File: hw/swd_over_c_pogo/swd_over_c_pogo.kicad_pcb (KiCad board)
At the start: 2 copper layers, 20.5 x 11 mm, 8 parts, among them J1 Conn_01x06

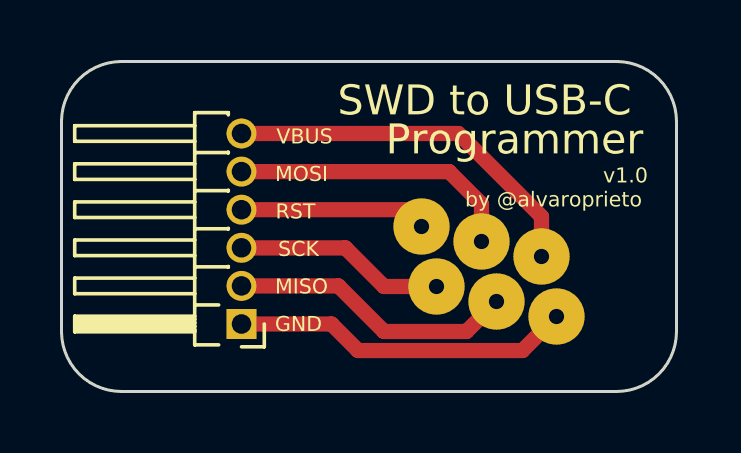
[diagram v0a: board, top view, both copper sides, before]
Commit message: Updated swd over c to v1.1 (and programmer)
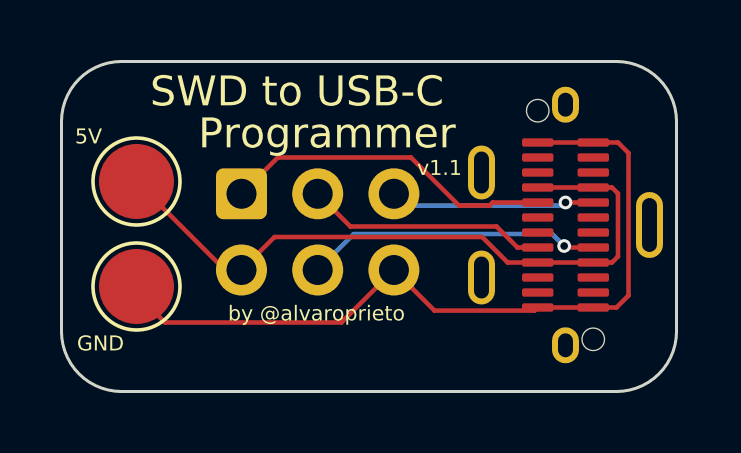
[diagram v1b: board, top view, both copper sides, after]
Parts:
- removed REF**: OSHW-Symbol_6.7x6mm_SilkScreen, Symbol:OSHW-Symbol_6.7x6mm_SilkScreen
- removed TP3: SCK, alvarop:0906-3-15-20-75-14-11-0
- removed TP4: MISO, alvarop:0906-3-15-20-75-14-11-0
- removed TP5: MOSI, alvarop:0906-3-15-20-75-14-11-0
- removed TP6: NRST, alvarop:0906-3-15-20-75-14-11-0
- added P1: USB_C_Plug, alvarop:USB4151-GF-C, F.Cu at (175.8, 67.5)
- J1: value Conn_01x06 -> AVR-ISP-6; footprint Connector_PinHeader_1.27mm:PinHeader_1x06_P1.27mm_Horizontal -> Connector_IDC:IDC-Header_2x03_P2.54mm_Vertical; moved to B.Cu
- TP1: value VBUS -> TestPoint; footprint alvarop:0906-3-15-20-75-14-11-0 -> TestPoint:TestPoint_Pad_D2.5mm
- TP2: value GND -> TestPoint; footprint alvarop:0906-3-15-20-75-14-11-0 -> TestPoint:TestPoint_Pad_D2.5mm
- moved TP2 14.0 mm to (161.5, 69.5), turned to -90 degrees
- moved TP1 13.7 mm to (161.5, 66.0), turned to -90 degrees
- moved J1 4.34 mm to (165.0, 66.4), turned to -90 degrees
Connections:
- J1 pad 1: GND -> /MISO
- J1 pad 2: /MISO -> VBUS
- J1 pad 4: /MCURST -> /MOSI
- J1 pad 5: /MOSI -> /MCURST
- J1 pad 6: VBUS -> GND
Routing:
- net GND: track 11.3 -> 25.9 mm
- net VBUS: track 12.5 -> 23.3 mm
- net /MISO: track 9.54 -> 11.1 mm
- net /SCK: track 7.03 -> 8.08 mm
- net /MCURST: track 6.23 -> 6.85 mm, vias 0 -> 1
- net /MOSI: track 9.70 -> 9.87 mm, vias 0 -> 1
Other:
- board text added: "5V"
- board text added: "v1.1"
- board text removed: "MISO"
- board text removed: "MOSI"
- board text removed: "RST"
- board text removed: "SCK"
- board text removed: "VBUS"
- board text removed: "v1.0"

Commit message: Switched to 0402 instead of 0201 components
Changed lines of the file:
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@@
     (fp_line (start -1.98 -8.99) (end -1.98 -4.59) (layer "B.Fab") (width 0.1))
     (fp_line (start -1.98 -4.59) (end -3.18 -4.59) (layer "B.Fab") (width 0.1))
-    (pad "1" thru_hole roundrect (at 0 0 270) (size 1.7 1.7) (drill 1) (layers *.Cu *.Mask) (roundrect_rratio 0.147059)
+    (pad "1" thru_hole roundrect (at 0 0 270) (size 1.7 1.7) (drill 1) (layers *.Cu *.Mask) (roundrect_rratio 0.1470588235)
       (net 3 "/MISO") (pinfunction "MISO") (pintype "passive"))
     (pad "2" thru_hole circle (at 2.54 0 270) (size 1.7 1.7) (drill 1) (layers *.Cu *.Mask)

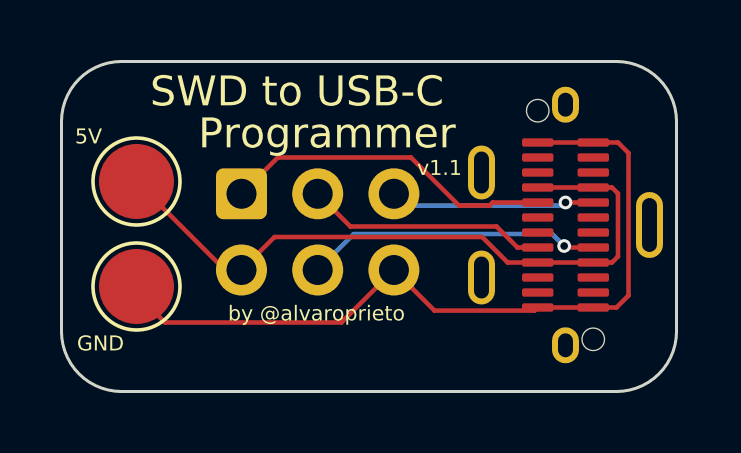
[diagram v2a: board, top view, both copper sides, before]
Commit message: Fixed MISO/MOSI swap and added BOM to swd2usbc
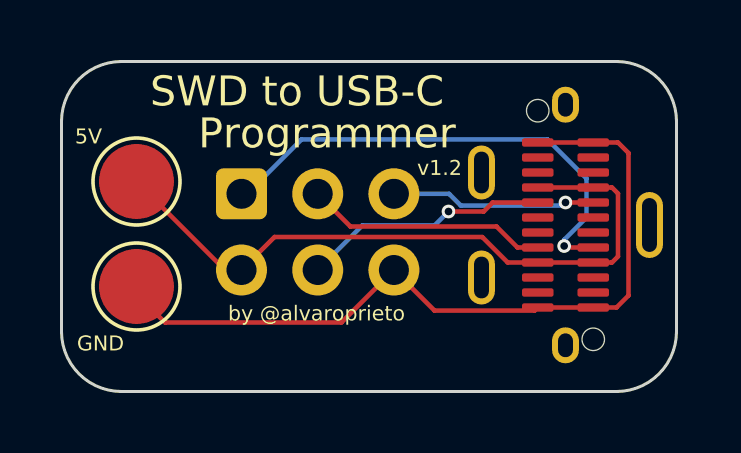
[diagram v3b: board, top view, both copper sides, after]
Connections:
- P1 pad A5: /MISO -> /MOSI
- P1 pad B5: /MOSI -> /MISO
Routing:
- net /MISO: track 11.1 -> 16.3 mm, vias 0 -> 1
- net /MOSI: track 9.87 -> 8.27 mm
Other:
- board text added: "v1.2"
- board text removed: "v1.1"
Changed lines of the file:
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@@
   (title_block
     (title "Debugotron - SWD to USB-C Programmer")
-    (date "2022-02-06")
-    (rev "1.1")
+    (date "2022-03-04")
+    (rev "1.2")
     (company "Quesadillon LLC")
   )
@@
   (footprint "alvarop:USB4151-GF-C" (layer "F.Cu")
     (at 175.8 67.45 90)
+    (property "MPN" " USB4151-GF-C")
     (property "Sheetfile" "swd_over_c_pogo.kicad_sch")
     (property "Sheetname" "")
@@
       (net 1 "VBUS") (pinfunction "VBUS") (pintype "passive"))
     (pad "A5" smd roundrect (at 0.75 -0.925 90) (size 0.28 1.05) (layers "F.Cu" "F.Paste" "F.Mask") (roundrect_rratio 0.25)
-      (net 3 "/MISO") (pinfunction "CC") (pintype "bidirectional"))
+      (net 4 "/MOSI") (pinfunction "CC") (pintype "bidirectional"))
     (pad "A6" smd roundrect (at 0.25 -0.925 90) (size 0.28 1.05) (layers "F.Cu" "F.Paste" "F.Mask") (roundrect_rratio 0.25)
       (net 9 "unconnected-(P1-PadA6)") (pinfunction "D+") (pintype "bidirectional+no_connect"))
@@
       (net 1 "VBUS") (pinfunction "VBUS") (pintype "passive"))
     (pad "B5" smd roundrect (at -0.75 0.925 90) (size 0.28 1.05) (layers "F.Cu" "F.Paste" "F.Mask") (roundrect_rratio 0.25)
-      (net 4 "/MOSI") (pinfunction "VCONN") (pintype "bidirectional"))
+      (net 3 "/MISO") (pinfunction "VCONN") (pintype "bidirectional"))
     (pad "B8" smd roundrect (at 0.75 0.925 90) (size 0.28 1.05) (layers "F.Cu" "F.Paste" "F.Mask") (roundrect_rratio 0.25)
       (net 6 "/MCURST") (pinfunction "SBU2") (pintype "bidirectional"))
@@
     (descr "Through hole IDC box header, 2x03, 2.54mm pitch, DIN 41651 / IEC 60603-13, double rows, https://docs.google.com/spreadsheets/d/16SsEcesNF15N3Lb4niX7dcUr-NY5_MFPQhobNuNppn4/edit#gid=0")
     (tags "Through hole vertical IDC box header THT 2x03 2.54mm double row")
+    (property "MPN" "30306-6002HB")
     (property "Sheetfile" "swd_over_c_pogo.kicad_sch")
     (property "Sheetname" "")
@@
     (effects (font (size 0.5 0.5) (thickness 0.08)))
   )
-  (gr_text "v1.1" (at 171.6 65.55) (layer "F.SilkS")
+  (gr_text "v1.2" (at 171.6 65.55) (layer "F.SilkS")
     (effects (font (size 0.5 0.5) (thickness 0.08)))
   )
@@
   (segment (start 174.875 70.2) (end 176.725 70.2) (width 0.1524) (layer "F.Cu") (net 2))
   (segment (start 171.43272 70.30272) (end 170.08 68.95) (width 0.1524) (layer "F.Cu") (net 2))
-  (segment (start 172.25272 66.80272) (end 170.65 65.2) (width 0.1524) (layer "F.Cu") (net 3))
-  (segment (start 174.875 66.7) (end 173.373085 66.7) (width 0.1524) (layer "F.Cu") (net 3))
-  (segment (start 166.21 65.2) (end 165 66.41) (width 0.1524) (layer "F.Cu") (net 3))
-  (segment (start 173.270365 66.80272) (end 172.25272 66.80272) (width 0.1524) (layer "F.Cu") (net 3))
-  (segment (start 173.373085 66.7) (end 173.270365 66.80272) (width 0.1524) (layer "F.Cu") (net 3))
-  (segment (start 170.65 65.2) (end 166.21 65.2) (width 0.1524) (layer "F.Cu") (net 3))
-  (segment (start 175.8051 68.2) (end 175.7551 68.15) (width 0.1524) (layer "F.Cu") (net 4))
-  (segment (start 176.725 68.2) (end 175.8051 68.2) (width 0.1524) (layer "F.Cu") (net 4))
-  (via (at 175.7551 68.15) (size 0.4572) (drill 0.254) (layers "F.Cu" "B.Cu") (net 4))
-  (segment (start 168.74 67.75) (end 167.54 68.95) (width 0.1524) (layer "B.Cu") (net 4))
-  (segment (start 175.7551 68.15) (end 175.3551 67.75) (width 0.1524) (layer "B.Cu") (net 4))
-  (segment (start 175.3551 67.75) (end 168.74 67.75) (width 0.1524) (layer "B.Cu") (net 4))
+  (segment (start 175.8051 68.2) (end 175.7551 68.15) (width 0.1524) (layer "F.Cu") (net 3))
+  (segment (start 176.725 68.2) (end 175.8051 68.2) (width 0.1524) (layer "F.Cu") (net 3))
+  (via (at 175.7551 68.15) (size 0.4572) (drill 0.254) (layers "F.Cu" "B.Cu") (net 3))
+  (segment (start 175.7551 67.9449) (end 176.5 67.2) (width 0.1524) (layer "B.Cu") (net 3))
+  (segment (start 175.7551 68.15) (end 175.7551 67.9449) (width 0.1524) (layer "B.Cu") (net 3))
+  (segment (start 167.00272 64.59728) (end 165.19 66.41) (width 0.1524) (layer "B.Cu") (net 3))
+  (segment (start 176.5 65.9) (end 175.19728 64.59728) (width 0.1524) (layer "B.Cu") (net 3))
+  (segment (start 165.19 66.41) (end 165 66.41) (width 0.1524) (layer "B.Cu") (net 3))
+  (segment (start 176.5 67.2) (end 176.5 65.9) (width 0.1524) (layer "B.Cu") (net 3))
+  (segment (start 175.19728 64.59728) (end 167.00272 64.59728) (width 0.1524) (layer "B.Cu") (net 3))
+  (segment (start 173.373085 66.7) (end 173.073085 67) (width 0.1524) (layer "F.Cu") (net 4))
+  (segment (start 174.875 66.7) (end 173.373085 66.7) (width 0.1524) (layer "F.Cu") (net 4))
+  (segment (start 173.073085 67) (end 171.9 67) (width 0.1524) (layer "F.Cu") (net 4))
+  (via (at 171.9 67) (size 0.4572) (drill 0.254) (layers "F.Cu" "B.Cu") (net 4))
+  (segment (start 171.437289 67.462711) (end 169.027289 67.462711) (width 0.1524) (layer "B.Cu") (net 4))
+  (segment (start 169.027289 67.462711) (end 167.54 68.95) (width 0.1524) (layer "B.Cu") (net 4))
+  (segment (start 171.9 67) (end 171.437289 67.462711) (width 0.1524) (layer "B.Cu") (net 4))
   (segment (start 174.875 68.2) (end 174.2 68.2) (width 0.1524) (layer "F.Cu") (net 5))
   (segment (start 168.63 67.5) (end 167.54 66.41) (width 0.1524) (layer "F.Cu") (net 5))
@@
   (segment (start 176.725 66.7) (end 175.8 66.7) (width 0.1524) (layer "F.Cu") (net 6))
   (via (at 175.8 66.7) (size 0.4572) (drill 0.254) (layers "F.Cu" "B.Cu") (net 6))
-  (segment (start 170.47272 66.80272) (end 170.08 66.41) (width 0.1524) (layer "B.Cu") (net 6))
-  (segment (start 175.69728 66.80272) (end 170.47272 66.80272) (width 0.1524) (layer "B.Cu") (net 6))
+  (segment (start 172.312673 66.80272) (end 171.919953 66.41) (width 0.1524) (layer "B.Cu") (net 6))
+  (segment (start 175.69728 66.80272) (end 172.312673 66.80272) (width 0.1524) (layer "B.Cu") (net 6))
   (segment (start 175.8 66.7) (end 175.69728 66.80272) (width 0.1524) (layer "B.Cu") (net 6))
+  (segment (start 171.919953 66.41) (end 170.08 66.41) (width 0.1524) (layer "B.Cu") (net 6))
 )

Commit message: Make USB over C programmer v2.0 for JLC
Hopefully it works
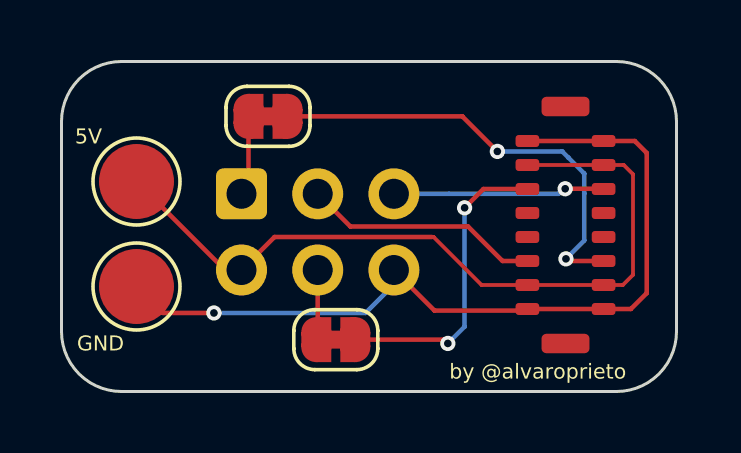
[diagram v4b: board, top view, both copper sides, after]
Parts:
- added JP1: MOSI, Jumper:SolderJumper-2_P1.3mm_Bridged_RoundedPad1.0x1.5mm, F.Cu at (165.9, 63.8)
- added JP2: MISO, Jumper:SolderJumper-2_P1.3mm_Bridged_RoundedPad1.0x1.5mm, F.Cu at (168.1, 71.3)
- P1: footprint alvarop:USB4151-GF-C -> alvarop:TYPE-C-31-G-06
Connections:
- J1 pad 1: /MISO -> /MISO_SRC
- J1 pad 4: /MOSI -> /MOSI_SRC
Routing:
- net VBUS: track 23.3 -> 26.0 mm
- net /MISO_SRC: track 0.00 -> 2.68 mm
- net /MOSI_SRC: track 0.00 -> 2.34 mm
- net GND: track 25.9 -> 27.9 mm, vias 0 -> 1
- net /MOSI: track 8.27 -> 10.2 mm, vias 1 -> 2
- net /MISO: track 16.3 -> 15.1 mm, vias 1 -> 2
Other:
- board text added: "SWD to USB-C Programmer"
- board text added: "v2.0"
- board text removed: "Programmer"
- board text removed: "SWD to USB-C"
- board text removed: "v1.2"

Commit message: Update footprint for USB plug
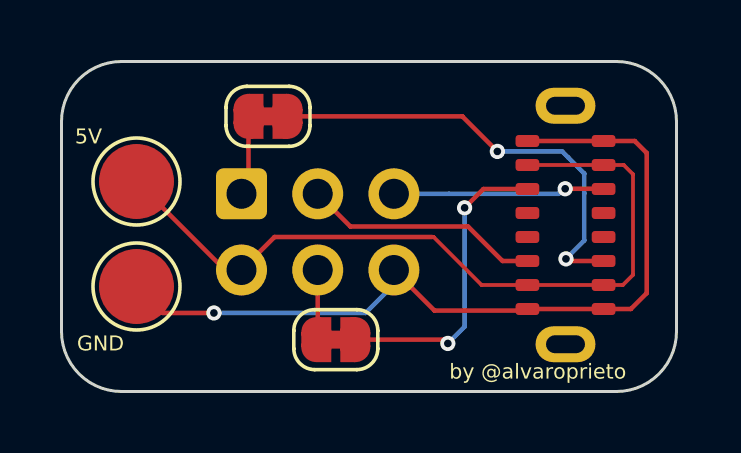
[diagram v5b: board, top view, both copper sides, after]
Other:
- board text added: "v2.1"
- board text removed: "v2.0"
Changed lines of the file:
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@@
     (title "Debugotron - SWD to USB-C Programmer")
     (date "2022-11-22")
-    (rev "2.0")
+    (rev "2.1")
     (company "Quesadillon LLC")
   )
@@
     (pad "B12" smd roundrect (at 2.8 1.27 90) (size 0.4 0.79) (layers "F.Cu" "F.Paste" "F.Mask") (roundrect_rratio 0.25)
       (net 2 "GND") (pinfunction "GND") (pintype "passive"))
-    (pad "S1" smd roundrect (at 3.95 0 90) (size 0.65 1.6) (layers "F.Cu" "F.Paste" "F.Mask") (roundrect_rratio 0.25)
+    (pad "S1" thru_hole oval (at 3.975 0 90) (size 1.2 2) (drill oval 0.6 1.3) (layers *.Cu *.Mask)
       (net 11 "unconnected-(P1-PadS1)") (pinfunction "SHIELD") (pintype "passive+no_connect"))
-    (pad "S1" smd roundrect (at -3.95 0 90) (size 0.65 1.6) (layers "F.Cu" "F.Paste" "F.Mask") (roundrect_rratio 0.25)
+    (pad "S1" thru_hole oval (at -3.975 0 90) (size 1.2 2) (drill oval 0.6 1.3) (layers *.Cu *.Mask)
       (net 11 "unconnected-(P1-PadS1)") (pinfunction "SHIELD") (pintype "passive+no_connect"))
   )
@@
   (gr_line (start 179.5 71) (end 179.5 64) (layer "Edge.Cuts") (width 0.1))
   (gr_line (start 177.5 62) (end 161 62) (layer "Edge.Cuts") (width 0.1))
-  (gr_text "SWD to USB-C\nProgrammer" (at 177.415 71.9314 270) (layer "B.SilkS")
+  (gr_text "SWD to USB-C\nProgrammer" (at 178.0246 71.9314 270) (layer "B.SilkS")
     (effects (font (size 0.762 0.762) (thickness 0.108857)) (justify left mirror))
   )
-  (gr_text "v2.0" (at 176.6784 63.651 270) (layer "B.SilkS")
+  (gr_text "v2.1" (at 177.288 63.651 270) (layer "B.SilkS")
     (effects (font (size 0.5 0.5) (thickness 0.08)) (justify mirror))
   )
